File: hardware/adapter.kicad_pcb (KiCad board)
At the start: 4 copper layers, 62 x 59 mm, 92 parts, among them J1 112-024-113R001, J2 HR871150C, J3 USB-C, J4 PWR_SEL, M1 DP9900LPB-5V1.4A, Q1 AO3401A, Q2 2N7002, U1 RP2354A, U2 W5500, U3 SN75160BDW, U4 SN75161BDW, U5 AP2114H-3.3TRG1, U6 TPS3839G33DBZR, X1 12MHz, X2 25MHz

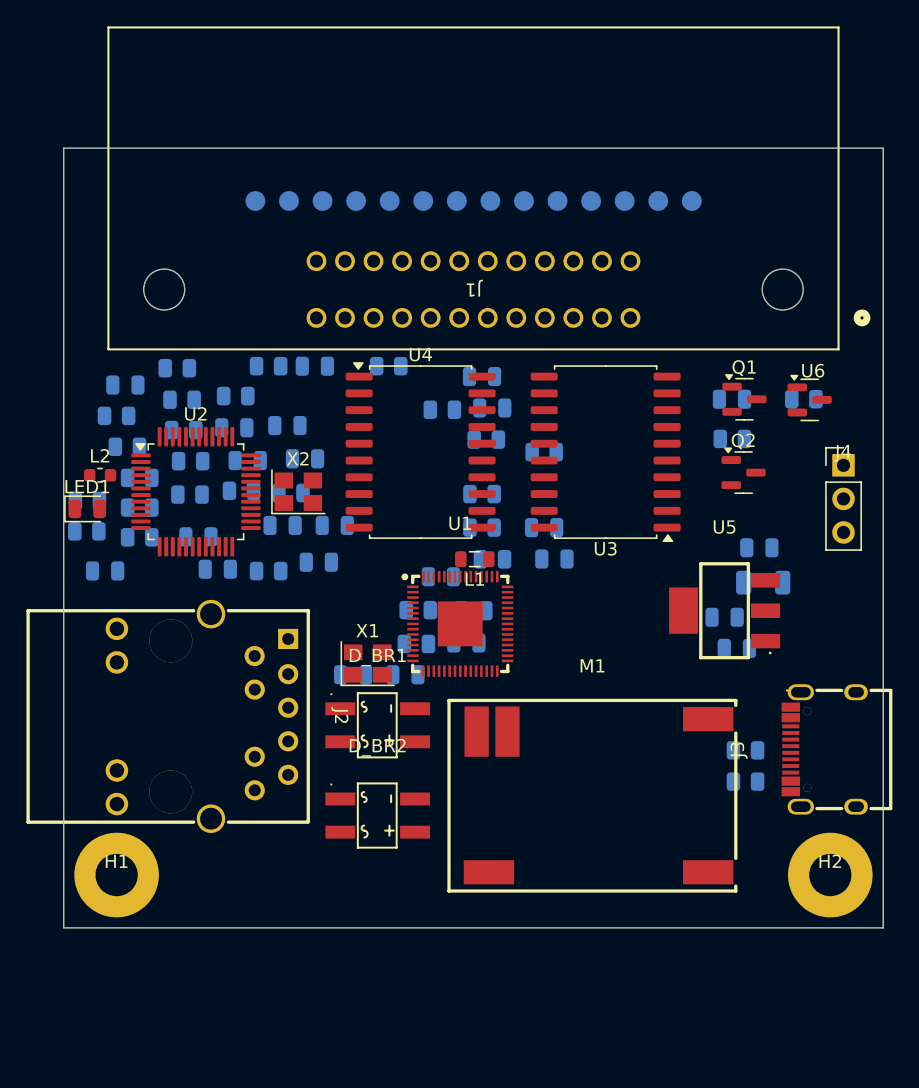
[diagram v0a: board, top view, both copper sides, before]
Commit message: hardware: updated board design (reference renumbering, LED polarity fix, crystal symbol upgrade)
Replaces the schematics/PCB/project file with the latest design. Key
changes, verified before committing (netlist-check.py: 124 checks, 0
failures; ERC unchanged at 3 known pin_not_driven findings on W5500 SPI
inputs, same severity-policy artifact as before):

- Component reference designators changed from descriptive names
  (R_ATN, C_3V3, D_BR1, etc.) to plain auto-numbered ones (R15, C9, D1,
  etc.) -- intentional, since descriptive names were ending up on the
  silkscreen; they belong in the BOM instead. docs/netlist-spec.nets
  updated to match via a UUID-verified old-ref -> new-ref mapping (every
  renamed symbol's KiCad UUID was unchanged, confirming these are pure
  renames with no electrical difference), not a hand transcription.
- LED1's wiring was corrected: the old schematic had its anode tied to
  GND and cathode driven by LED_A (backwards -- confirmed via each net's
  pinfunction annotation in the exported netlist, K_1/A_2, which is
  fixed by the Device:LED symbol regardless of reference numbering).
  The new schematic has cathode-to-GND, anode-to-LED_A, the correct
  orientation.
- X1/X2 changed from Device:Crystal (2-pin) to Device:Crystal_GND24
  (4-pin, case-ground on pins 2/4) -- a more accurate symbol for the
  real SMD crystal package. netlist-spec.nets updated accordingly
  (XOUT/ETH_XO now reference pin 3, GND gained the four case pins).

mcu.kicad_sch was supplied separately (missing from the first archive);
confirmed it has no further sub-sheet references and all its symbols'
footprint names resolve against the existing hardware/lib/adapter.pretty/
library, which was deliberately left untouched along with fp-lib-table,
sym-lib-table, and .konnect/ -- none of those changed in this update.
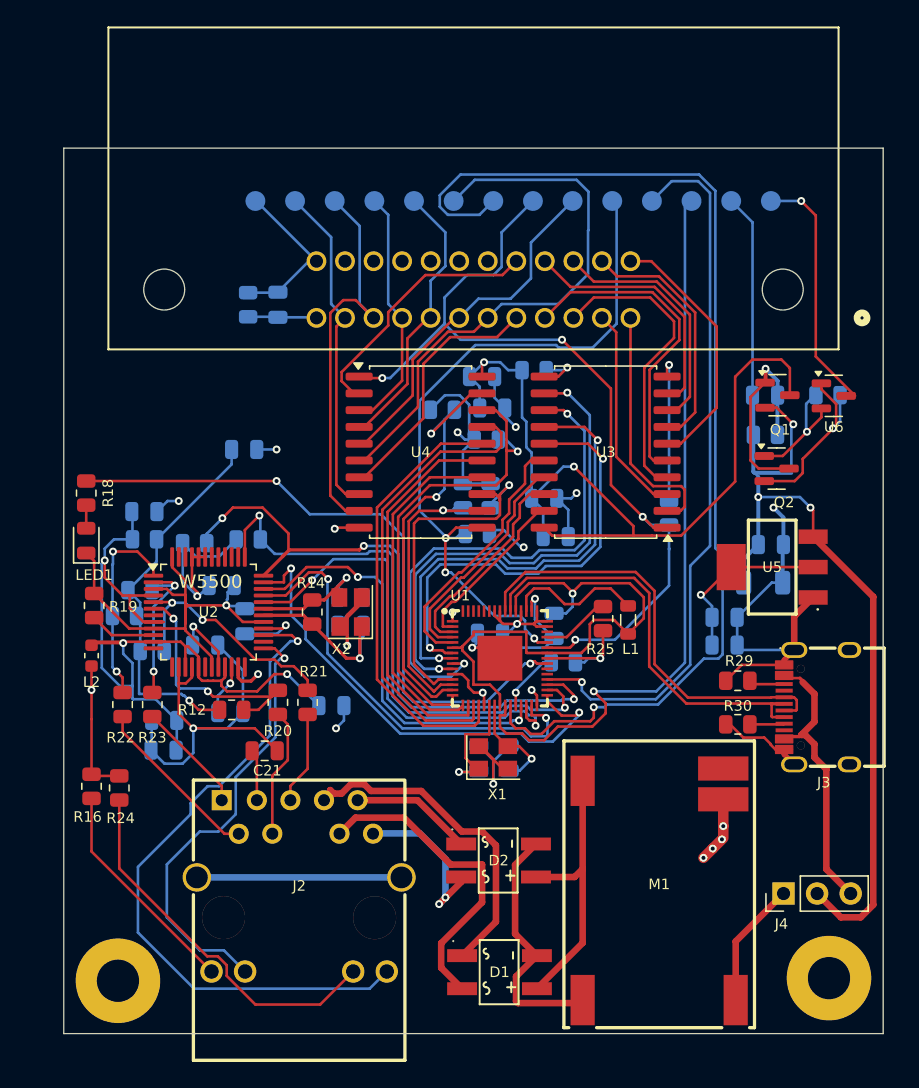
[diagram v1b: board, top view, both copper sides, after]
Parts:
- C21: renamed from C_RCT1; moved to F.Cu
- R12: renamed from R_T4; moved to F.Cu
- R14: renamed from R_XF1; moved to F.Cu
- R16: renamed from R_LEDL1; moved to F.Cu
- R18: renamed from R_LED1; moved to F.Cu
- R19: renamed from RSET1; moved to F.Cu
- R20: renamed from R_RX2; moved to F.Cu
- R21: renamed from R_RX1; moved to F.Cu
- R22: renamed from R_TX1; moved to F.Cu
- R23: renamed from R_TX2; moved to F.Cu
- R24: renamed from R_LEDR1; moved to F.Cu
- R25: renamed from R_CFG1; moved to F.Cu
- R29: renamed from R_CC2; moved to F.Cu
- R30: renamed from R_CC1; moved to F.Cu
- moved TP_3V3 36.5 mm to (153.5, 64.0)
- moved J4 32.7 mm to (154.5, 116.4), turned to 90 degrees
- moved TP_5V1 30.9 mm to (150.5, 64.0)
- moved TP_SWCLK1 25.4 mm to (147.5, 64.0)
- moved C10 24.5 mm to (107.5, 105.5), turned to 180 degrees
- moved C8 24.2 mm to (107.6, 103.3), turned to 180 degrees
- moved R2 23.9 mm to (145.8, 87.6), turned to 90 degrees
- moved R23 22.0 mm to (106.7, 102.1), turned to -90 degrees
- moved R16 21.6 mm to (102.1, 108.3), turned to -90 degrees
- moved R22 21.3 mm to (104.5, 102.1), turned to -90 degrees
- moved C22 21.2 mm to (113.7, 82.8)
- moved D1 20.8 mm to (133.0, 122.3)
- moved R21 20.3 mm to (118.5, 101.9), turned to -90 degrees
- moved R24 19.9 mm to (104.2, 108.4), turned to -90 degrees
- moved C21 18.2 mm to (115.2, 105.6)
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- renumbered C_SH1 to C1, C_ETHc1 to C10, C_ETHbulk1 to C11, C_U3a1 to C12, C_TOCAP1 to C13, C_X2a1 to C14, C_X2b1 to C15, C_LDOin1 to C16, C_U3b1 to C17, C_ETHa1 to C18, C_1V2O1 to C19, C_U4a1 to C2, C_BULK1 to C20, C_BIAS1 to C22, C_3V3 to C23, C_LDOout1 to C24, C_X1a1 to C25, C_X1b1 to C26, C_ETHb1 to C3, C_G1 to C4, C_U4b1 to C5, C_ETHd1 to C8, C_VDD1 to C9, D_BR1 to D1, D_BR2 to D2, R_SH1 to R1, R_T2 to R10, R_PE1 to R11, R_T1 to R13, R_ATN1 to R15, R_T3 to R17, R_TE1 to R2, R_SRQ1 to R26, R_RUN1 to R27, R_DC1 to R28, R_B1 to R3, R_RSTP1 to R4, R_INTP1 to R5, R_G2 to R6, R_REN1 to R7, R_G1 to R8, R_IFC1 to R9
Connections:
- net /Ethernet W5500 and magjack/ETH_RXN_W renamed /Ethernet W5500 and magjack/ETH_RXWN
- net /Ethernet W5500 and magjack/ETH_RXP_W renamed /Ethernet W5500 and magjack/ETH_RXWP
- net /Ethernet W5500 and magjack/ETH_TXN_W renamed /Ethernet W5500 and magjack/ETH_TXWN
- net /Ethernet W5500 and magjack/ETH_TXP_W renamed /Ethernet W5500 and magjack/ETH_TXWP
- net /MCU RP2354A/USB_DM renamed /MCU RP2354A/USB_DN
- LED1 pad 1: /MCU RP2354A/LED_A -> GND
- LED1 pad 2: GND -> /MCU RP2354A/LED_A
- X1 pad 2: /MCU RP2354A/XOUT -> GND
- X1 pad 3: (no net) -> /MCU RP2354A/XOUT
- X1 pad 4: (no net) -> GND
- X2 pad 2: /Ethernet W5500 and magjack/ETH_XO -> GND
- X2 pad 3: (no net) -> /Ethernet W5500 and magjack/ETH_XO
- X2 pad 4: (no net) -> GND
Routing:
- net GND: track 0.00 -> 217.5 mm, vias 0 -> 20
- net +3V3: track 0.00 -> 104.0 mm, vias 0 -> 12
- net /MCU RP2354A/SWDIO: track 0.00 -> 83.6 mm, vias 0 -> 1
- net +5V_SYS: track 0.00 -> 81.0 mm, vias 0 -> 3
- net /GPIB transceivers and IEEE-488 connector/TE: track 0.00 -> 66.9 mm, vias 0 -> 4
- net +5V_XCVR: track 0.00 -> 64.3 mm, vias 0 -> 2
- net /Ethernet W5500 and magjack/3V3A: track 0.00 -> 63.5 mm, vias 0 -> 3
- net /MCU RP2354A/SWCLK: track 0.00 -> 56.3 mm, vias 0 -> 1
- net /GPIB transceivers and IEEE-488 connector/DC: track 0.00 -> 55.8 mm, vias 0 -> 3
- net /MCU RP2354A/TP_SPARE: track 0.00 -> 54.6 mm, vias 0 -> 1
- net /Ethernet W5500 and magjack/ETH_ACTLED: track 0.00 -> 51.8 mm, vias 0 -> 1
- net /MCU RP2354A/LED_DRV: track 0.00 -> 50.0 mm, vias 0 -> 2
- net /Ethernet W5500 and magjack/ETH_INTn: track 0.00 -> 49.0 mm, vias 0 -> 3
- net /Ethernet W5500 and magjack/ETH_RSTn: track 0.00 -> 43.0 mm, vias 0 -> 2
- net /GPIB transceivers and IEEE-488 connector/DAV_B: track 0.00 -> 42.6 mm
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- added copper zone on In2.Cu, net +3V3
- added copper zone on In1.Cu, net GND
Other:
- board size 62 x 59 mm -> 62 x 67 mm
